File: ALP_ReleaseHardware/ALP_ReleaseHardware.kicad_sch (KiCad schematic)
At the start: 13 parts

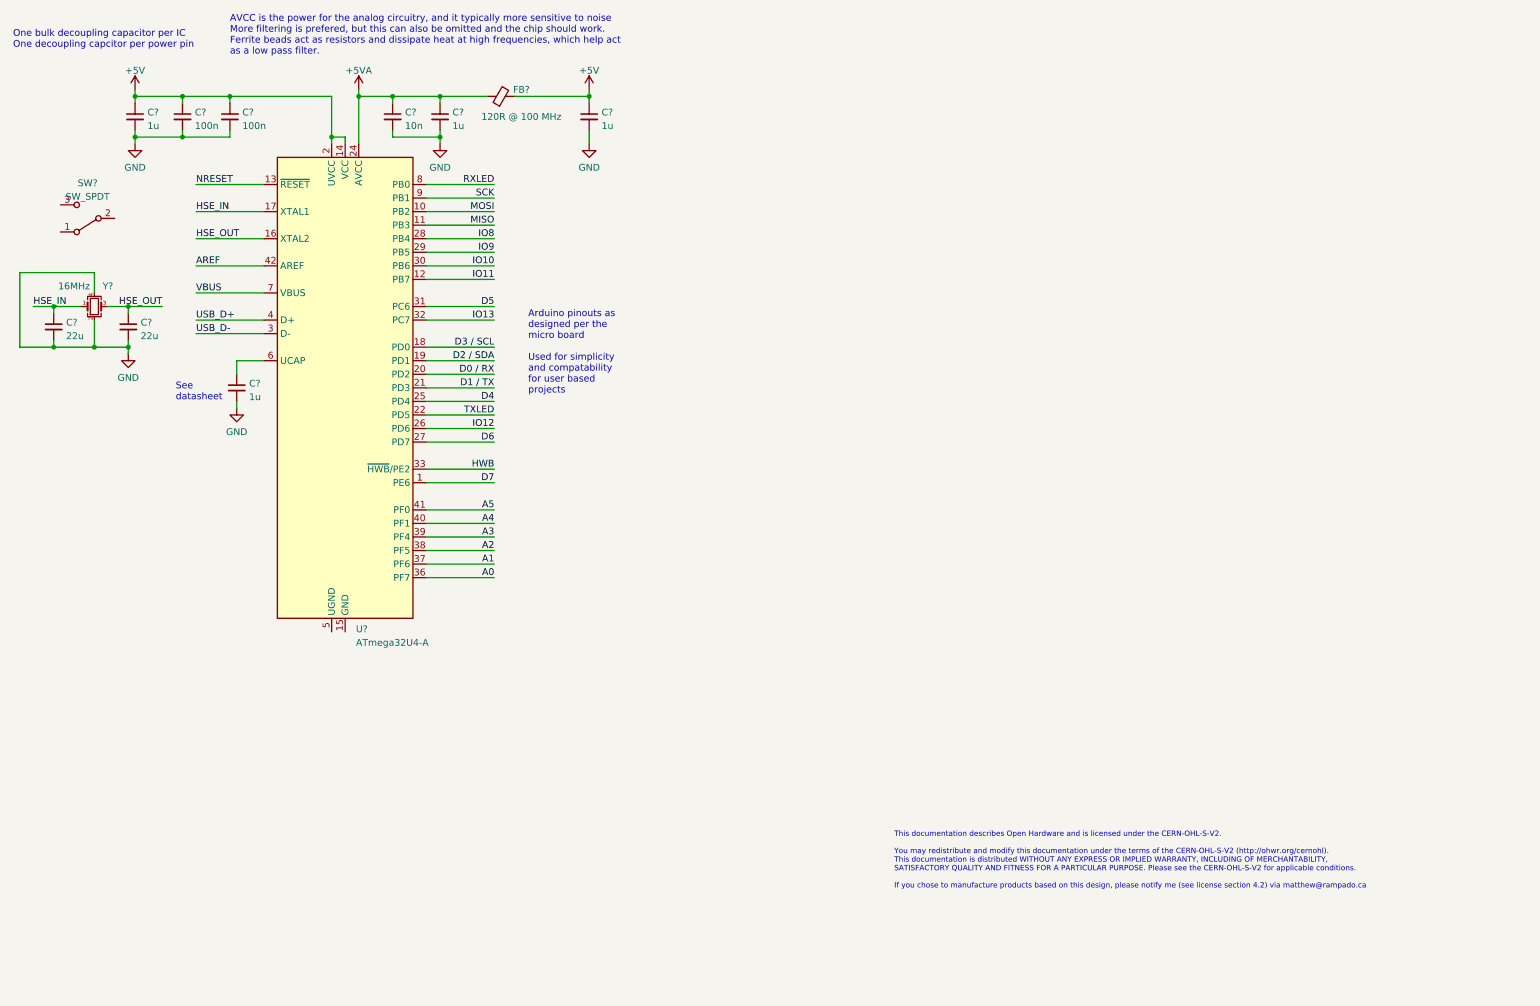
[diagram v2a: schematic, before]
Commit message: Added USBC and ISP Programming Header
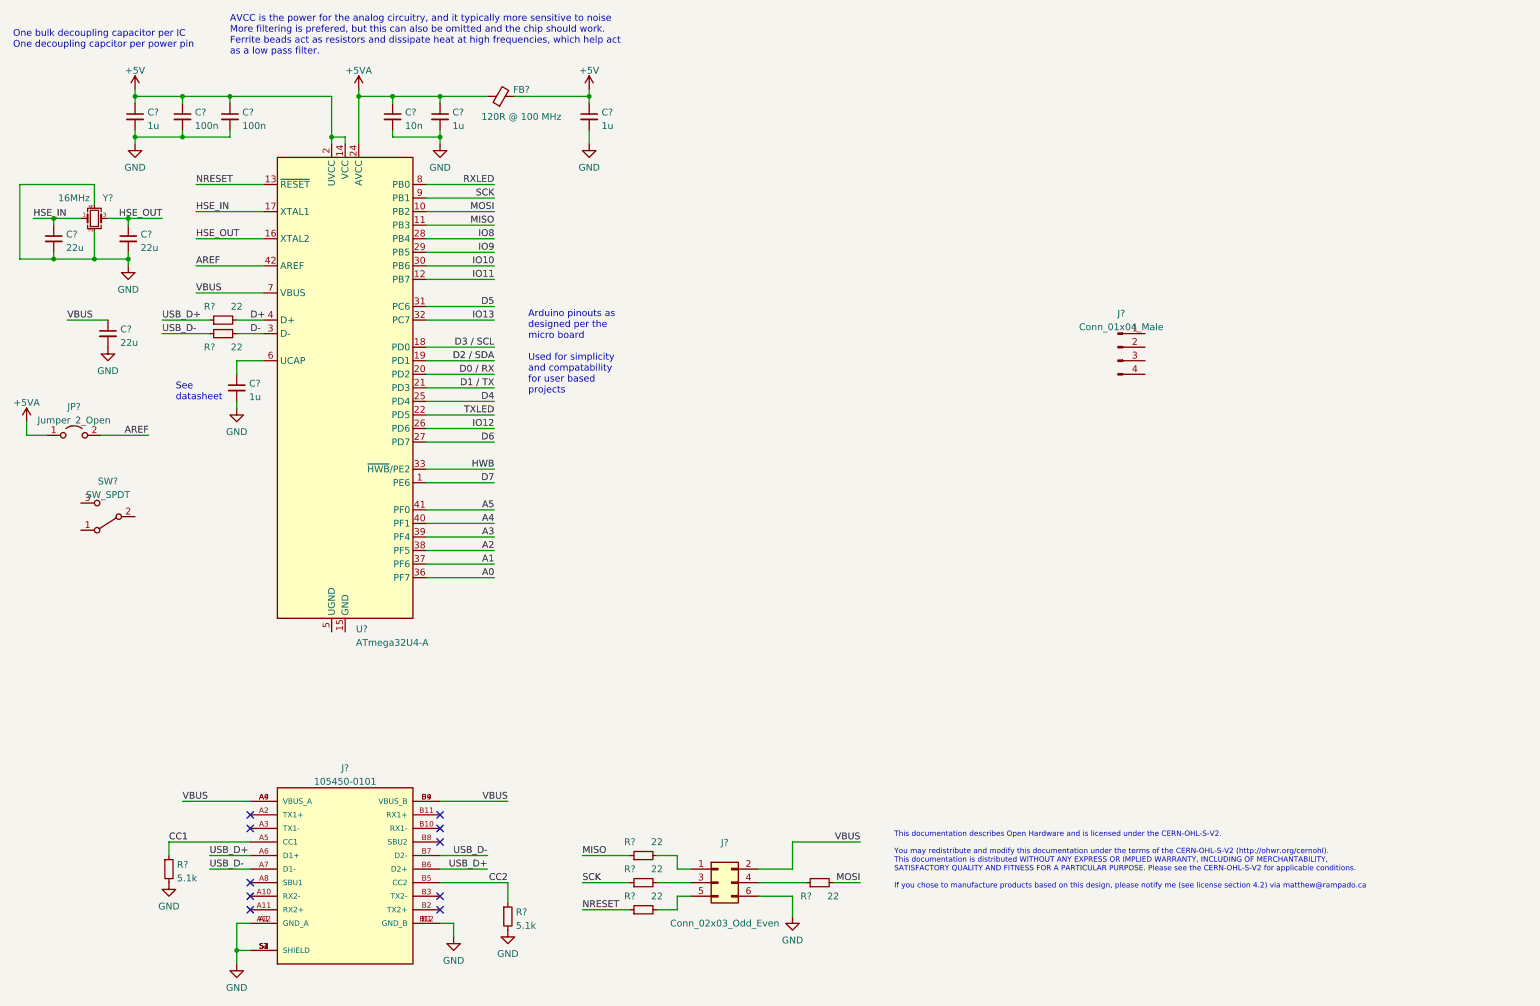
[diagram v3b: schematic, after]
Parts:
- added C?: 22u, symbol Device:C_Small
- added J?: 105450-0101, MOLEX_105450-0101, symbol Rampado_Master:105450-0101
- added J?: Conn_02x03_Odd_Even, symbol Connector_Generic:Conn_02x03_Odd_Even
- added J?: Conn_01x04_Male, symbol Connector:Conn_01x04_Male
- added JP?: Jumper_2_Open, symbol Jumper:Jumper_2_Open
- added R? (x6): 22, symbol Device:R_Small
- added R? (x2): 5.1k, symbol Device:R_Small
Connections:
- net +5VA: now also JP?.1 (A)
- net AREF: now also JP?.2 (B)
- net GND: now also C?.2, J?.6 (Pin_6), J?.A1 (GND_A), J?.A12 (GND_A), J?.B1 (GND_B), J?.B12 (GND_B), J?.S1 (SHIELD), J?.S2 (SHIELD), J?.S3 (SHIELD), J?.S4 (SHIELD), R?.2, R?.2
- net MISO: now also R?.1
- net MOSI: now also R?.2
- net NRESET: now also R?.1
- net SCK: now also R?.1
- net USB_D+: now also J?.A6 (D1+), J?.B6 (D2+), R?.1; no longer U?.4 (D+)
- net USB_D-: now also J?.A7 (D1-), J?.B7 (D2-), R?.1; no longer U?.3 (D-)
- net VBUS: now also C?.1, J?.2 (Pin_2), J?.A4 (VBUS_A), J?.A9 (VBUS_A), J?.B4 (VBUS_B), J?.B9 (VBUS_B)
- new net: J?.5 (Pin_5), R?.2
- new net: J?.1 (Pin_1), R?.2
- new net: J?.3 (Pin_3), R?.2
- new net: J?.4 (Pin_4), R?.1
- new net CC1: J?.A5 (CC1), R?.1
- new net CC2: J?.B5 (CC2), R?.1
- new net D+: R?.2, U?.4 (D+)
- new net D-: R?.2, U?.3 (D-)
- no-connect marks 0 -> 10
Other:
- moved on the sheet: C?, SW?, Y?

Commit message: Added LEDs, footprints, and part#s to schematic
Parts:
- removed J?: Conn_01x04_Male, symbol Connector:Conn_01x04_Male
- added D?: RED, LED_SMD:LED_0603_1608Metric_Pad1.05x0.95mm_HandSolder, symbol Device:LED
- added D? (x3): YELLOW, LED_SMD:LED_0603_1608Metric_Pad1.05x0.95mm_HandSolder, symbol Device:LED
- added D?: BLUE, LED_SMD:LED_0603_1608Metric_Pad1.05x0.95mm_HandSolder, symbol Device:LED
- added D? (x2): GREEN, LED_SMD:LED_0603_1608Metric_Pad1.05x0.95mm_HandSolder, symbol Device:LED
- added D?: WHITE, LED_SMD:LED_0603_1608Metric_Pad1.05x0.95mm_HandSolder, symbol Device:LED
- added R? (x8): 1k, Resistor_SMD:R_0603_1608Metric_Pad0.98x0.95mm_HandSolder, symbol Device:R_Small
- C? (x4): footprint (none) -> Capacitor_SMD:C_0603_1608Metric_Pad1.08x0.95mm_HandSolder; JLCPCB Part # (none) -> C15849
- C? (x3): footprint (none) -> Capacitor_SMD:C_0603_1608Metric_Pad1.08x0.95mm_HandSolder; JLCPCB Part # (none) -> C59461
- C? (x2): footprint (none) -> Capacitor_SMD:C_0603_1608Metric_Pad1.08x0.95mm_HandSolder; JLCPCB Part # (none) -> C14663
- C?: footprint (none) -> Capacitor_SMD:C_0603_1608Metric_Pad1.08x0.95mm_HandSolder; JLCPCB Part # (none) -> C57112
- R? (x6): footprint (none) -> Resistor_SMD:R_0603_1608Metric_Pad0.98x0.95mm_HandSolder; JLCPCB Part # (none) -> C23345
- R? (x2): footprint (none) -> Resistor_SMD:R_0603_1608Metric_Pad0.98x0.95mm_HandSolder; JLCPCB Part # (none) -> C23186
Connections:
- net +5V: now also R?.1
- net D0 / RX: now also R?.1
- net D1 / TX: now also R?.1
- net GND: now also D?.1 (K), D?.1 (K), D?.1 (K), D?.1 (K), D?.1 (K), D?.1 (K), D?.1 (K), D?.1 (K)
- new net: D?.2 (A), R?.2 (x8)
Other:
- note added: "Place programming header on rear of PCB to keep out of the way. Can use POGO pins or similar to program"

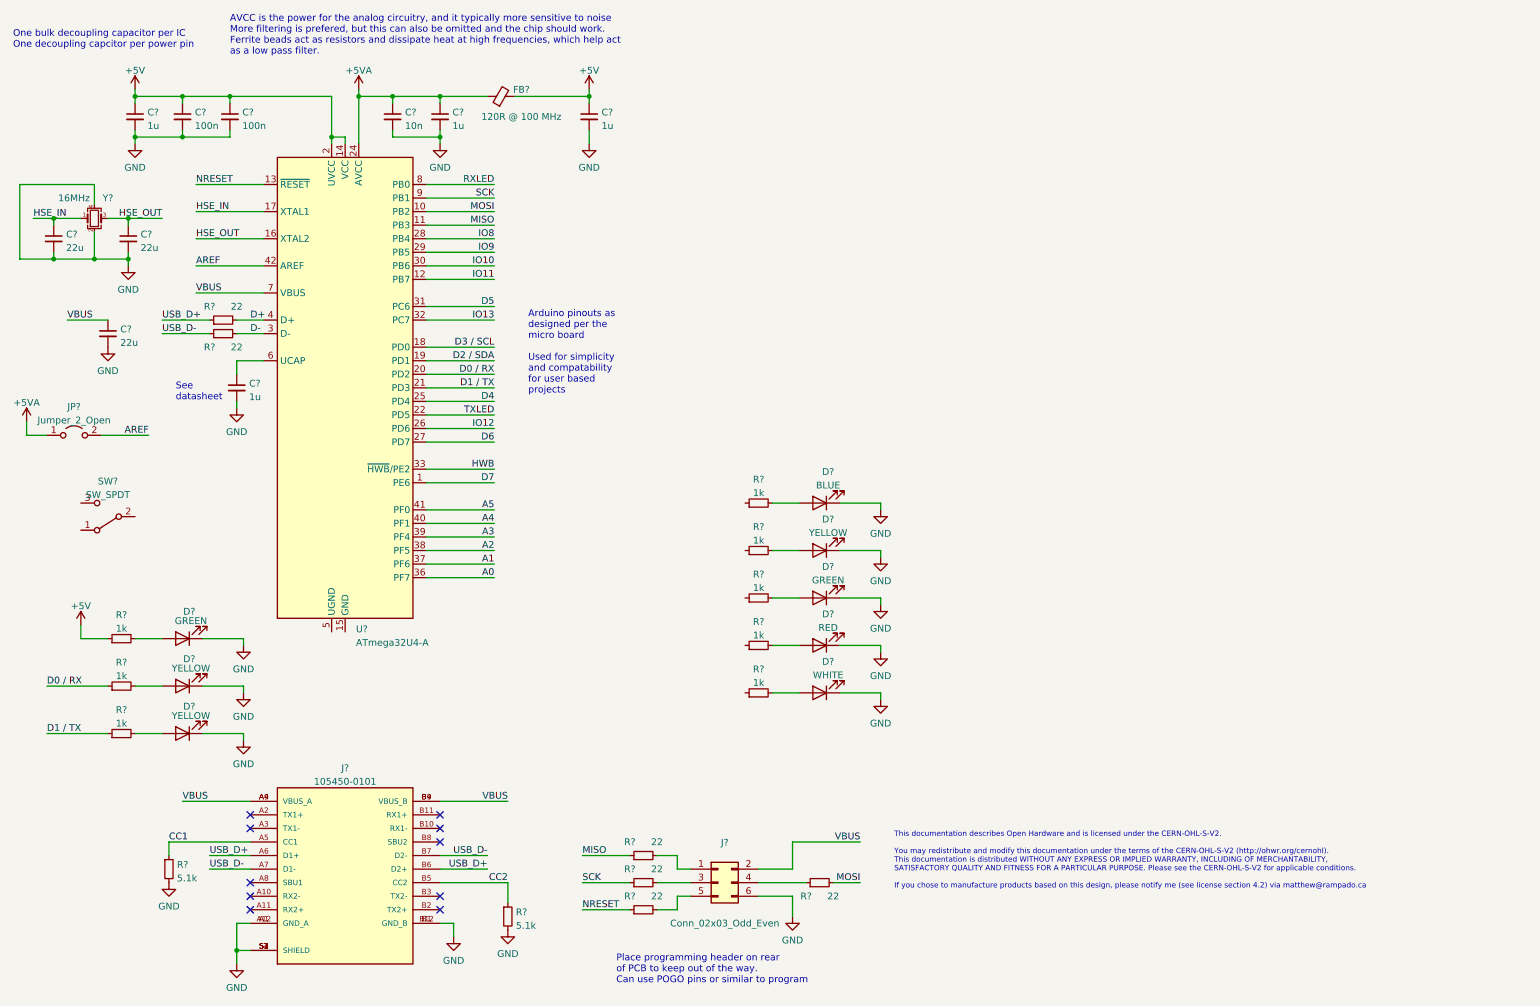
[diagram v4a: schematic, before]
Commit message: Power Protection Added
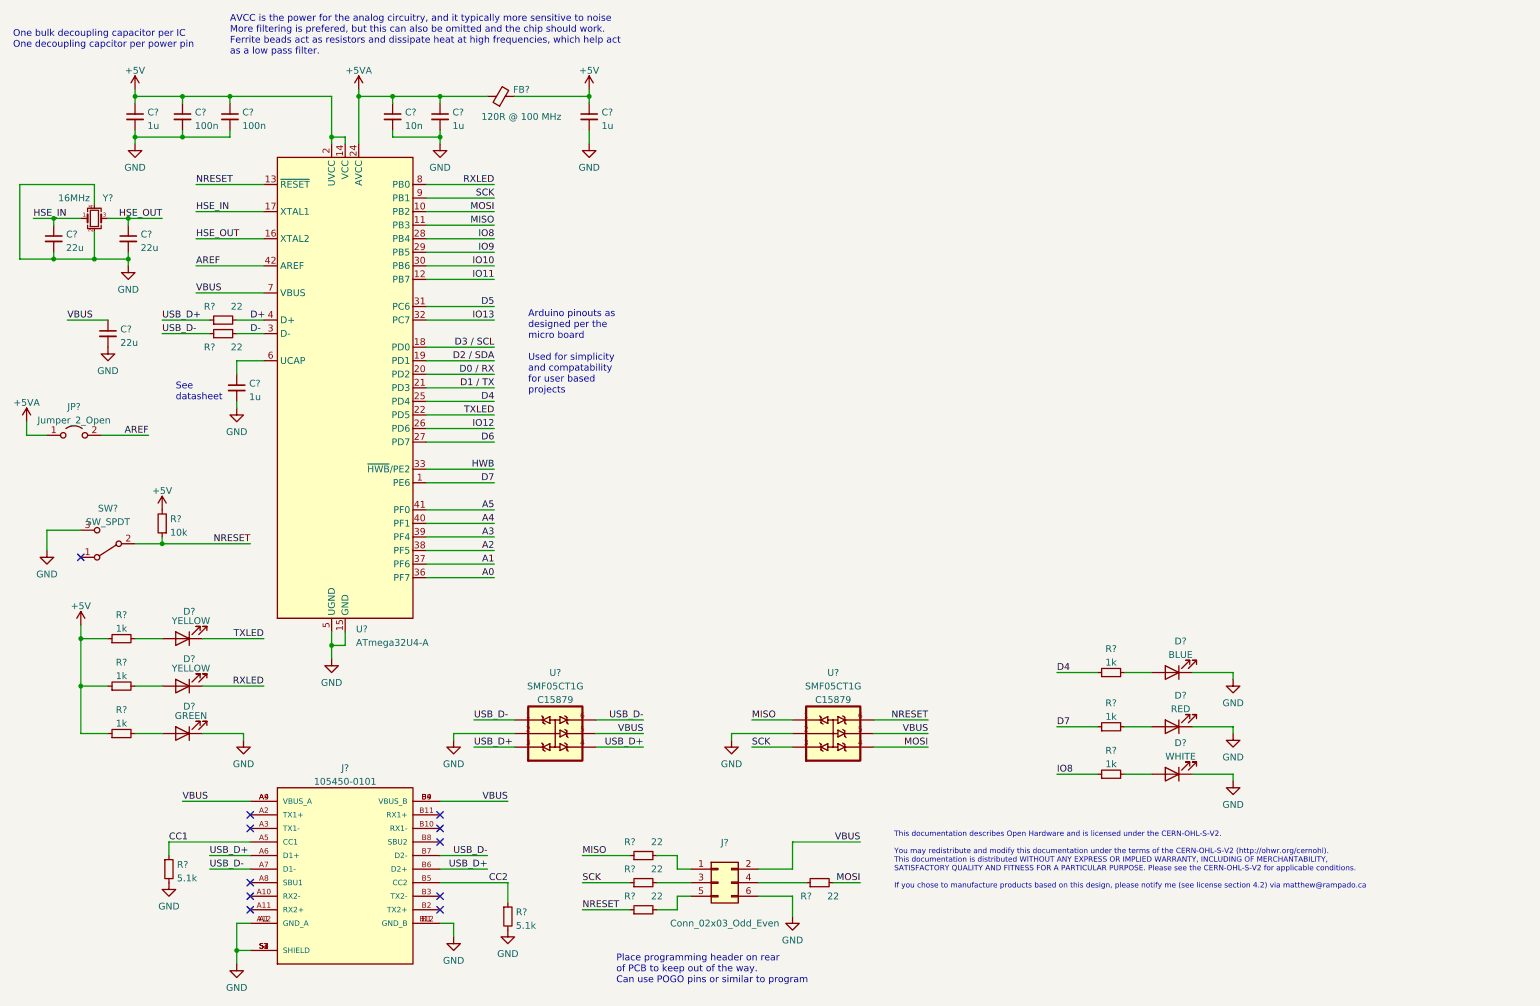
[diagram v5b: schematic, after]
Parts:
- removed D?: YELLOW, LED_SMD:LED_0603_1608Metric_Pad1.05x0.95mm_HandSolder, symbol Device:LED
- removed D?: GREEN, LED_SMD:LED_0603_1608Metric_Pad1.05x0.95mm_HandSolder, symbol Device:LED
- removed R? (x2): 1k, Resistor_SMD:R_0603_1608Metric_Pad0.98x0.95mm_HandSolder, symbol Device:R_Small
- added R?: 10k, Resistor_SMD:R_0603_1608Metric_Pad0.98x0.95mm_HandSolder, symbol Device:R_Small
- added U? (x2): SMF05CT1G, SOT65P210X110-6N, symbol Rampado_Master:SMF05CT1G
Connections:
- net +5V: now also R?.1, R?.1, R?.2
- net D0 / RX: no longer R?.1
- net D1 / TX: no longer R?.1
- net D4: now also R?.1
- net D7: now also R?.1
- net GND: now also SW?.3 (C), U?.15 (GND), U?.23 (GND), U?.35 (GND), U?.43 (GND), U?.5 (UGND), U?.2, U?.2; no longer D?.1 (K), D?.1 (K)
- net IO8: now also R?.1
- net MISO: now also U?.1
- net MOSI: now also U?.4
- net NRESET: now also SW?.2 (B), R?.1, U?.6
- net RXLED: now also D?.1 (K)
- net SCK: now also U?.3
- net TXLED: now also D?.1 (K)
- net USB_D+: now also U?.3, U?.4
- net USB_D-: now also U?.1, U?.6
- net VBUS: now also U?.5, U?.5
- net at R?.2: now also D?.2 (A); no longer D?.2 (A) (x2)
- no-connect marks 10 -> 11
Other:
- moved on the sheet: D?, R?, SW?

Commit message: Base Schematic Done before peripherals added
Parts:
- removed J?: 105450-0101, MOLEX_105450-0101, symbol Rampado_Master:105450-0101
- removed SW?: SW_SPDT, symbol Switch:SW_SPDT
- removed U?: ATmega32U4-A, Package_QFP:TQFP-44_10x10mm_P0.8mm, symbol MCU_Microchip_ATmega:ATmega32U4-A
- added J?: 105450-0101, MOLEX_105450-0101, symbol Rampado_Master:105450-0101
- added R? (x2): 10k, Resistor_SMD:R_0603_1608Metric_Pad0.98x0.95mm_HandSolder, symbol Device:R_Small
- added S? (x3): TS-1187A-B-A-B, SW_TS-1187A-B-A-B, symbol Rampado_Master:TS-1187A-B-A-B
- added U?: ATmega32U4-M, Package_DFN_QFN:QFN-44-1EP_7x7mm_P0.5mm_EP5.2x5.2mm, symbol MCU_Microchip_ATmega:ATmega32U4-M
- FB?: footprint (none) -> Inductor_SMD:L_0805_2012Metric_Pad1.05x1.20mm_HandSolder; JLCPCB Part # (none) -> C1015
- J?: footprint (none) -> Connector_PinHeader_2.54mm:PinHeader_2x03_P2.54mm_Vertical; JLCPCB Part # (none) -> C65114
- JP?: footprint (none) -> Jumper:SolderJumper-2_P1.3mm_Open_RoundedPad1.0x1.5mm; JLCPCB Part # (none) -> N/A
- Y?: footprint (none) -> Crystal:Crystal_SMD_3225-4Pin_3.2x2.5mm_HandSoldering; JLCPCB Part # (none) -> C112972
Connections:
- net +5V: now also R?.2, S?.C, S?.D, U?.14 (VCC), U?.2 (UVCC), U?.34 (VCC)
- net +5VA: now also U?.24 (AVCC), U?.44 (AVCC)
- net A0: now also U?.36 (PF7)
- net A1: now also U?.37 (PF6)
- net A2: now also U?.38 (PF5)
- net A3: now also U?.39 (PF4)
- net A4: now also R?.1, S?.A, S?.B, U?.40 (PF1)
- net A5: now also R?.2, S?.A, S?.B, U?.41 (PF0)
- net AREF: now also U?.42 (AREF)
- net CC1: now also J?.A5 (CC1)
- net CC2: now also J?.B5 (CC2)
- net D+: now also U?.4 (D+)
- net D-: now also U?.3 (D-)
- net D0 / RX: now also U?.20 (PD2)
- net D1 / TX: now also U?.21 (PD3)
- net D2 / SDA: now also U?.19 (PD1)
- net D3 / SCL: now also U?.18 (PD0)
- net D4: now also U?.25 (PD4)
- net D5: now also R?.1, U?.31 (PC6)
- net D6: now also U?.27 (PD7)
- net D7: now also U?.1 (PE6); no longer R?.1
- net GND: now also J?.A1 (GND_A), J?.A12 (GND_A), J?.B1 (GND_B), J?.B12 (GND_B), J?.S1 (SHIELD), J?.S2 (SHIELD), J?.S3 (SHIELD), J?.S4 (SHIELD), R?.1, S?.B, S?.C, S?.D, U?.15 (GND), U?.23 (GND), U?.35 (GND), U?.43 (GND), U?.45 (GND), U?.5 (UGND)
- net HSE_IN: now also U?.17 (XTAL1)
- net HSE_OUT: now also U?.16 (XTAL2)
- net HWB: now also U?.33 (~{HWB}/PE2)
- net IO10: now also U?.30 (PB6)
- net IO11: now also U?.12 (PB7)
- net IO12: now also U?.26 (PD6)
- net IO13: now also U?.32 (PC7)
- net IO8: now also U?.28 (PB4)
- net IO9: now also U?.29 (PB5)
- net MISO: now also U?.11 (PB3)
- net MOSI: now also U?.10 (PB2)
- net NRESET: now also S?.D, U?.13 (~{RESET})
- net RXLED: now also U?.8 (PB0)
- net SCK: now also U?.9 (PB1)
- net TXLED: now also U?.22 (PD5)
- net USB_D+: now also J?.A6 (D1+), J?.B6 (D2+)
- net USB_D-: now also J?.A7 (D1-), J?.B7 (D2-)
- net VBUS: now also J?.A4 (VBUS_A), J?.A9 (VBUS_A), J?.B4 (VBUS_B), J?.B9 (VBUS_B), U?.7 (VBUS)
- net at C?.1: now also U?.6 (UCAP)
- no-connect marks 11 -> 12
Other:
- moved on the sheet: R?

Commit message: Base Schematic Minor Edits
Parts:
- added R?: 10k, Resistor_SMD:R_0603_1608Metric_Pad0.98x0.95mm_HandSolder, symbol Device:R_Small
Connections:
- net GND: now also R?.2
- net HWB: now also R?.1
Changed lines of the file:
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@@
+    (stroke (width 0) (type default) (color 0 0 0 0))
+  )
+  (wire (pts (xy 25.4 167.64) (xy 16.51 167.64))
     (stroke (width 0) (type default) (color 0 0 0 0))
   )
@@
   )
   (wire (pts (xy 15.24 90.17) (xy 15.24 92.71))
+    (stroke (width 0) (type default) (color 0 0 0 0))
+  )
+  (wire (pts (xy 25.4 171.45) (xy 25.4 167.64))
     (stroke (width 0) (type default) (color 0 0 0 0))
   )
@@
   )
   (label "AREF" (at 46.99 60.96 0)
+    (effects (font (size 1.27 1.27)) (justify left bottom))
+  )
+  (label "HWB" (at 16.51 167.64 0)
     (effects (font (size 1.27 1.27)) (justify left bottom))
   )
@@
     (pin "S4")
   )
+  (symbol (lib_id "power:GND") (at 25.4 176.53 0) (unit 1)
+    (in_bom yes) (on_board yes) (fields_autoplaced)
+    (property "Reference" "#PWR?" (id 0) (at 25.4 182.88 0)
+      (effects (font (size 1.27 1.27)) hide)
+    )
+    (property "Value" "GND" (id 1) (at 25.4 180.9734 0))
+    (property "Footprint" "" (id 2) (at 25.4 176.53 0)
+      (effects (font (size 1.27 1.27)) hide)
+    )
+    (property "Datasheet" "" (id 3) (at 25.4 176.53 0)
+      (effects (font (size 1.27 1.27)) hide)
+    )
+    (pin "1")
+  )
   (symbol (lib_id "Rampado_Master:SMF05CT1G") (at 114.3 148.59 0) (unit 1)
     (in_bom yes) (on_board yes) (fields_autoplaced)
@@
     )
     (property "JLCPCB Part #" "C1015" (id 4) (at 104.14 29.21 0)
+      (effects (font (size 1.27 1.27)) hide)
+    )
+    (pin "1")
+    (pin "2")
+  )
+  (symbol (lib_id "Device:R_Small") (at 25.4 173.99 0) (unit 1)
+    (in_bom yes) (on_board yes) (fields_autoplaced)
+    (property "Reference" "R?" (id 0) (at 26.8986 173.1553 0)
+      (effects (font (size 1.27 1.27)) (justify left))
+    )
+    (property "Value" "10k" (id 1) (at 26.8986 175.6922 0)
+      (effects (font (size 1.27 1.27)) (justify left))
+    )
+    (property "Footprint" "Resistor_SMD:R_0603_1608Metric_Pad0.98x0.95mm_HandSolder" (id 2) (at 25.4 173.99 0)
+      (effects (font (size 1.27 1.27)) hide)
+    )
+    (property "Datasheet" "~" (id 3) (at 25.4 173.99 0)
+      (effects (font (size 1.27 1.27)) hide)
+    )
+    (property "JLCPCB Part #" "C23186" (id 4) (at 25.4 173.99 0)
       (effects (font (size 1.27 1.27)) hide)
     )
@@
       (reference "#PWR?") (unit 1) (value "GND") (footprint "")
     )
+    (path "/97b37ee1-a2a6-412b-abb5-a0dac9cbcda8"
+      (reference "#PWR?") (unit 1) (value "GND") (footprint "")
+    )
     (path "/acb6b1e0-ca27-4ab8-bfd1-3d0851328be6"
       (reference "#PWR?") (unit 1) (value "GND") (footprint "")
@@
       (reference "R?") (unit 1) (value "1k") (footprint "Resistor_SMD:R_0603_1608Metric_Pad0.98x0.95mm_HandSolder")
     )
+    (path "/b69f4a8b-4f10-4e19-b977-2c59101948ba"
+      (reference "R?") (unit 1) (value "10k") (footprint "Resistor_SMD:R_0603_1608Metric_Pad0.98x0.95mm_HandSolder")
+    )
     (path "/bd2dcd5a-9f80-4856-b435-b02eb787c151"
